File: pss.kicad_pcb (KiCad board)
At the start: 2 copper layers, 352 x 220 mm, 665 parts, among them J101 Conn_01x06_Socket, J102 Conn_01x02_Socket, J103 Conn_01x02_Socket, J104 Conn_01x02_Socket, J2001 Conn_01x06_Socket, J2002 Conn_01x06_Socket, J2101 Conn_01x06_Socket, J2801 Conn_01x06_Socket, K3501 ALFG2PF12, M2101 Fan, M2801 Fan, Q1401 DNLS350E, Q1901 DPLS350E, Q1902 DNLS350E, Q1903 DPLS350E, Q1904 DPLS350E, Q1905 DNLS350E, Q1906 DNLS350E, Q1907 TIP41C, Q1908 TIP42C, Q2201 DNLS350E, Q2202 DPLS350E, Q2203 TIP41C, Q2204 TIP42C, Q2301 DNLS350E, Q2302 DPLS350E, Q2303 TIP41C, Q2304 TIP42C, Q2401 DNLS350E, Q2402 DPLS350E, Q2403 TIP41C, Q2404 TIP42C, Q2501 DNLS350E, Q2502 DPLS350E, Q2503 TIP41C, Q2504 TIP42C, Q2601 DNLS350E, Q2602 DPLS350E, Q2603 TIP41C, Q2604 TIP42C, Q2701 DNLS350E, Q2702 DPLS350E, Q2703 TIP41C, Q2704 TIP42C, Q2901 DNLS350E, Q2902 DPLS350E, Q2903 TIP41C, Q2904 TIP42C, Q3001 DNLS350E, Q3002 DPLS350E, Q3003 TIP41C, Q3004 TIP42C, Q3101 DNLS350E, Q3102 DPLS350E, Q3103 TIP41C, Q3104 TIP42C, Q3201 DNLS350E, Q3202 DPLS350E, Q3203 TIP41C, Q3204 TIP42C, Q3301 DNLS350E, Q3302 DPLS350E, Q3303 TIP41C, Q3304 TIP42C, Q3401 DNLS350E, Q3402 DPLS350E, Q3403 TIP41C, Q3404 TIP42C, Q3501 DPLS350E, Q401 DNLS350E, Q402 DNLS350E, Q403 DPLS350E, Q404 DPLS350E, U1001 TLV9352, U1101 TLV9352, U1201 TLV9352, U1301 TLV9352, U1401 4081, U1402 4073, U1403 4073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

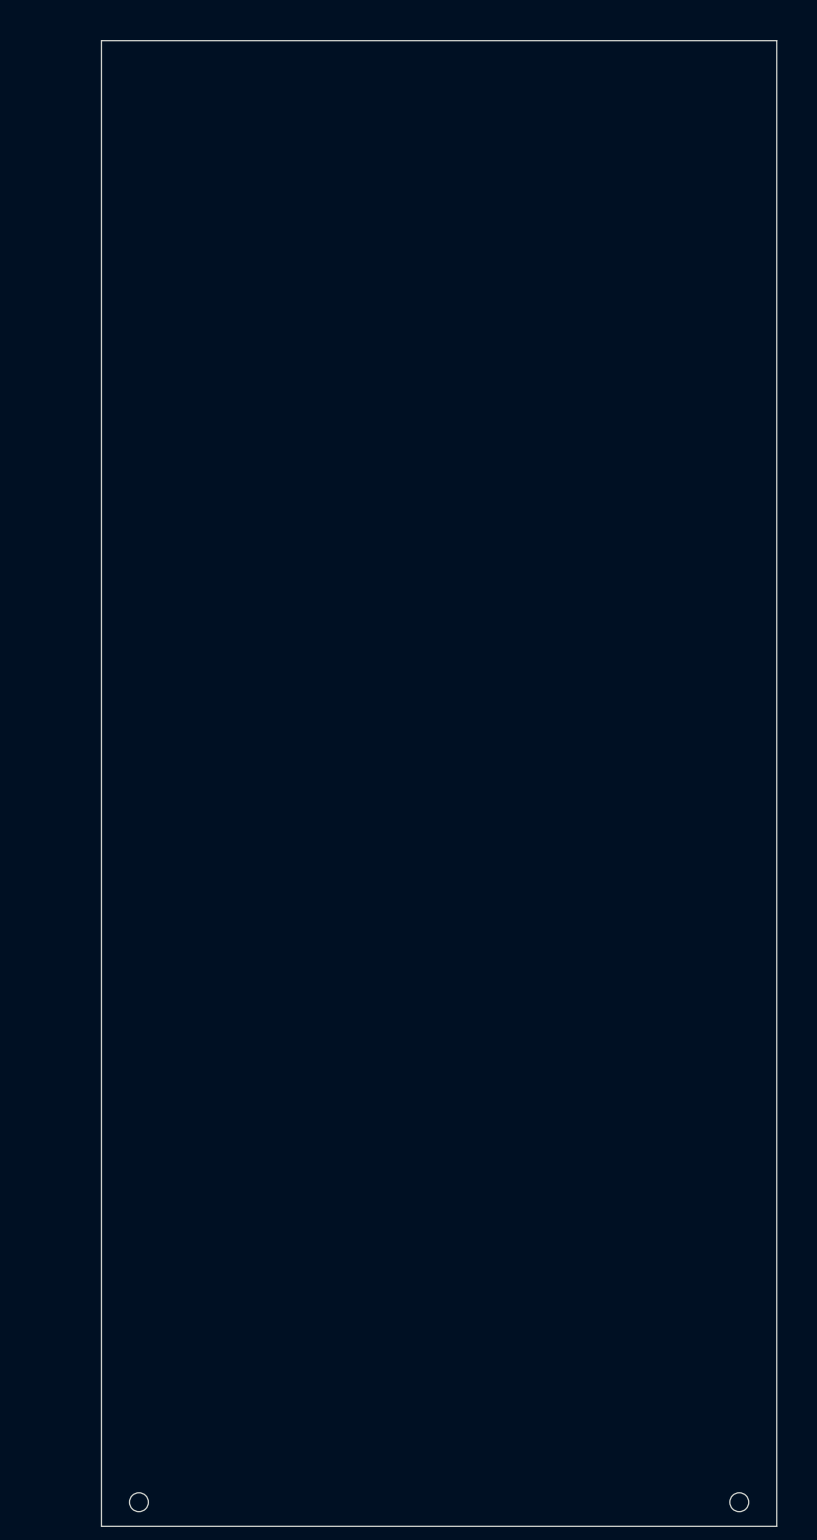
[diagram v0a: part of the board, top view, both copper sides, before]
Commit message: add pcb edge clearance keepout area
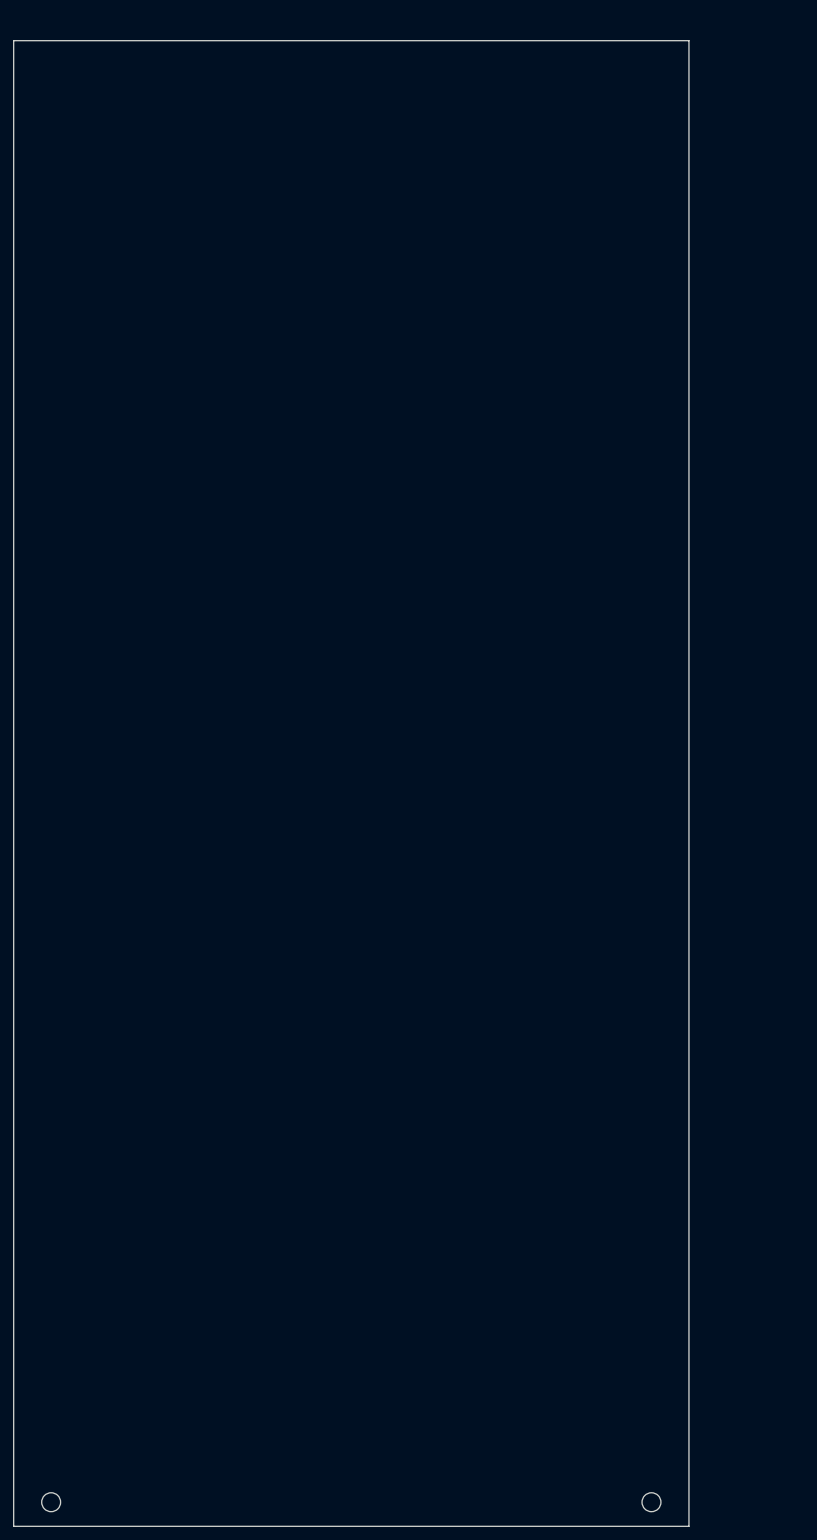
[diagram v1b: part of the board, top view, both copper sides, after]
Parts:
- moved REF** 13.0 mm to (129.4, 236.4)
- moved REF** 13.0 mm to (40.5, 236.4)
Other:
- board size 352 x 220 mm -> 365 x 220 mm

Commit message: add pcb mounting holes for stacking via M3x60 hexnuts
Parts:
- added REF**: MountingHole_3.2mm_M3, pss:MountingHole_3.2mm_M3, F.Cu at (320.0, 90.0)
- added REF**: MountingHole_3.2mm_M3, pss:MountingHole_3.2mm_M3, F.Cu at (380.0, 220.0)
- added REF**: MountingHole_3.2mm_M3, pss:MountingHole_3.2mm_M3, F.Cu at (380.0, 90.0)
- added REF**: MountingHole_3.2mm_M3, pss:MountingHole_3.2mm_M3, F.Cu at (205.0, 90.0)
- added REF**: MountingHole_3.2mm_M3, pss:MountingHole_3.2mm_M3, F.Cu at (205.0, 220.0)
- added REF**: MountingHole_3.2mm_M3, pss:MountingHole_3.2mm_M3, F.Cu at (320.0, 220.0)
- added REF**: MountingHole_3.2mm_M3, pss:MountingHole_3.2mm_M3, F.Cu at (115.0, 220.0)
- added REF**: MountingHole_3.2mm_M3, pss:MountingHole_3.2mm_M3, F.Cu at (55.0, 220.0)
- added REF**: MountingHole_3.2mm_M3, pss:MountingHole_3.2mm_M3, F.Cu at (55.0, 90.0)
- added REF**: MountingHole_3.2mm_M3, pss:MountingHole_3.2mm_M3, F.Cu at (265.0, 90.0)
- added REF**: MountingHole_3.2mm_M3, pss:MountingHole_3.2mm_M3, F.Cu at (115.0, 90.0)
- added REF**: MountingHole_3.2mm_M3, pss:MountingHole_3.2mm_M3, F.Cu at (265.0, 220.0)
- moved M2801 189.0 mm to (-3.88, -30.5), turned to 180 degrees
- moved JP2801 125.5 mm to (31.1, -73.8)
- moved TP2801 125.5 mm to (27.0, -74.0)
- moved TP2802 125.5 mm to (27.0, -71.0)
- moved TP2803 125.5 mm to (27.0, -67.9)
- moved TP2804 125.5 mm to (27.0, -64.8)
- moved TP2805 125.5 mm to (27.0, -61.8)
- moved TP2806 125.5 mm to (27.0, -58.8)
- moved HS2801 72.6 mm to (-3.88, -170.5)
- moved J2801 66.5 mm to (40.5, -111.7), turned to -90 degrees

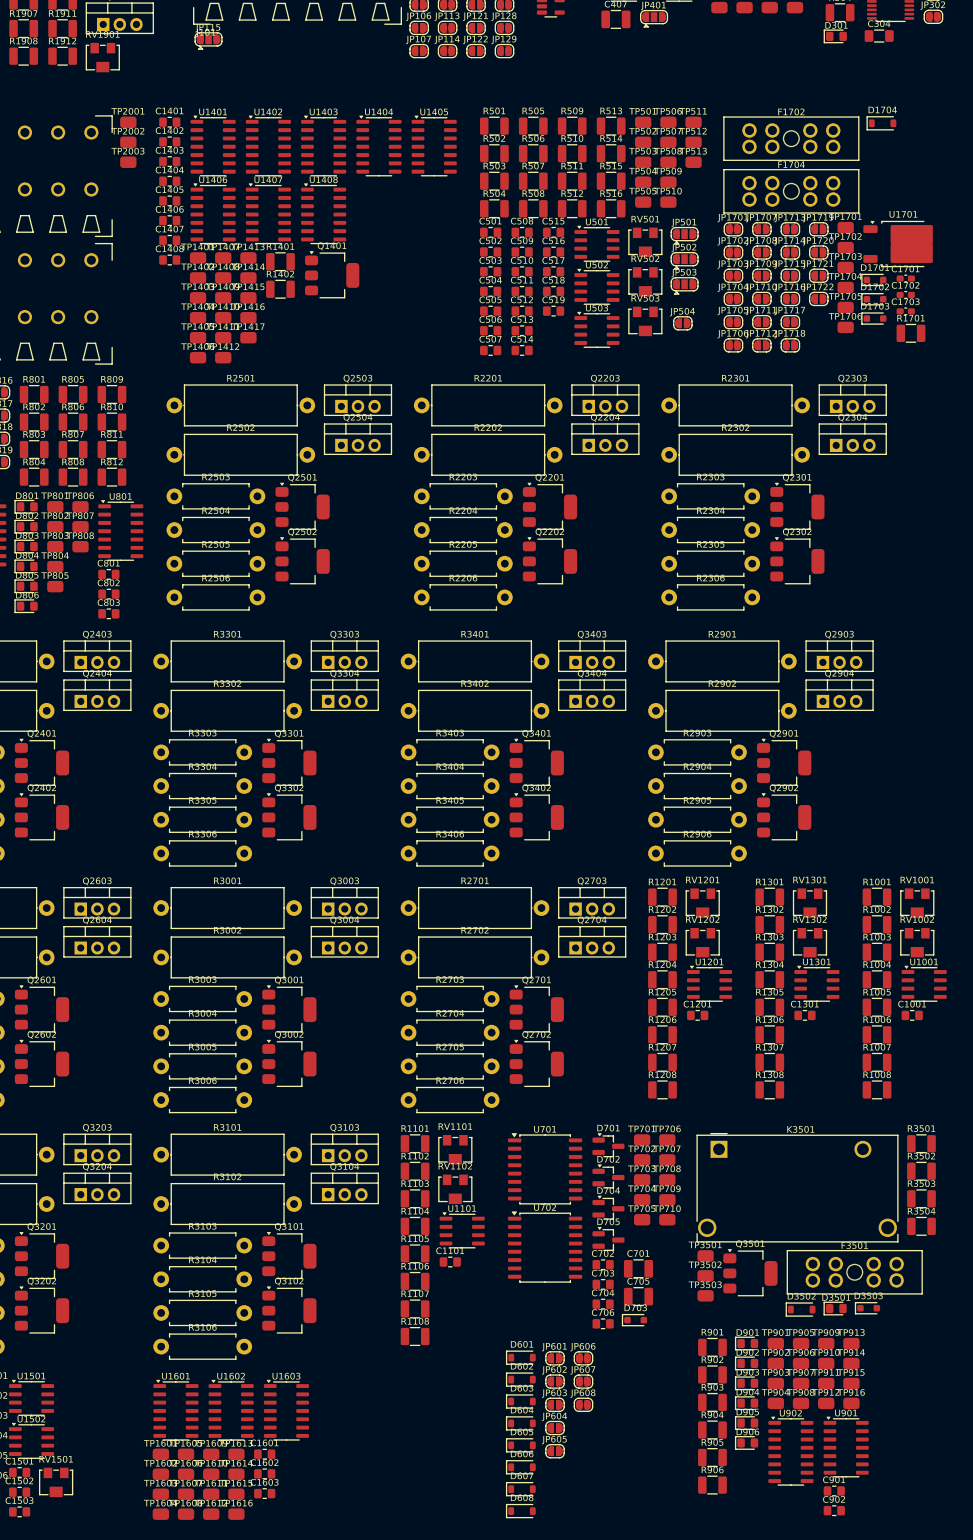
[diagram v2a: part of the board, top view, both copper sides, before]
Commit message: edit trimmer adjustment style to sideways
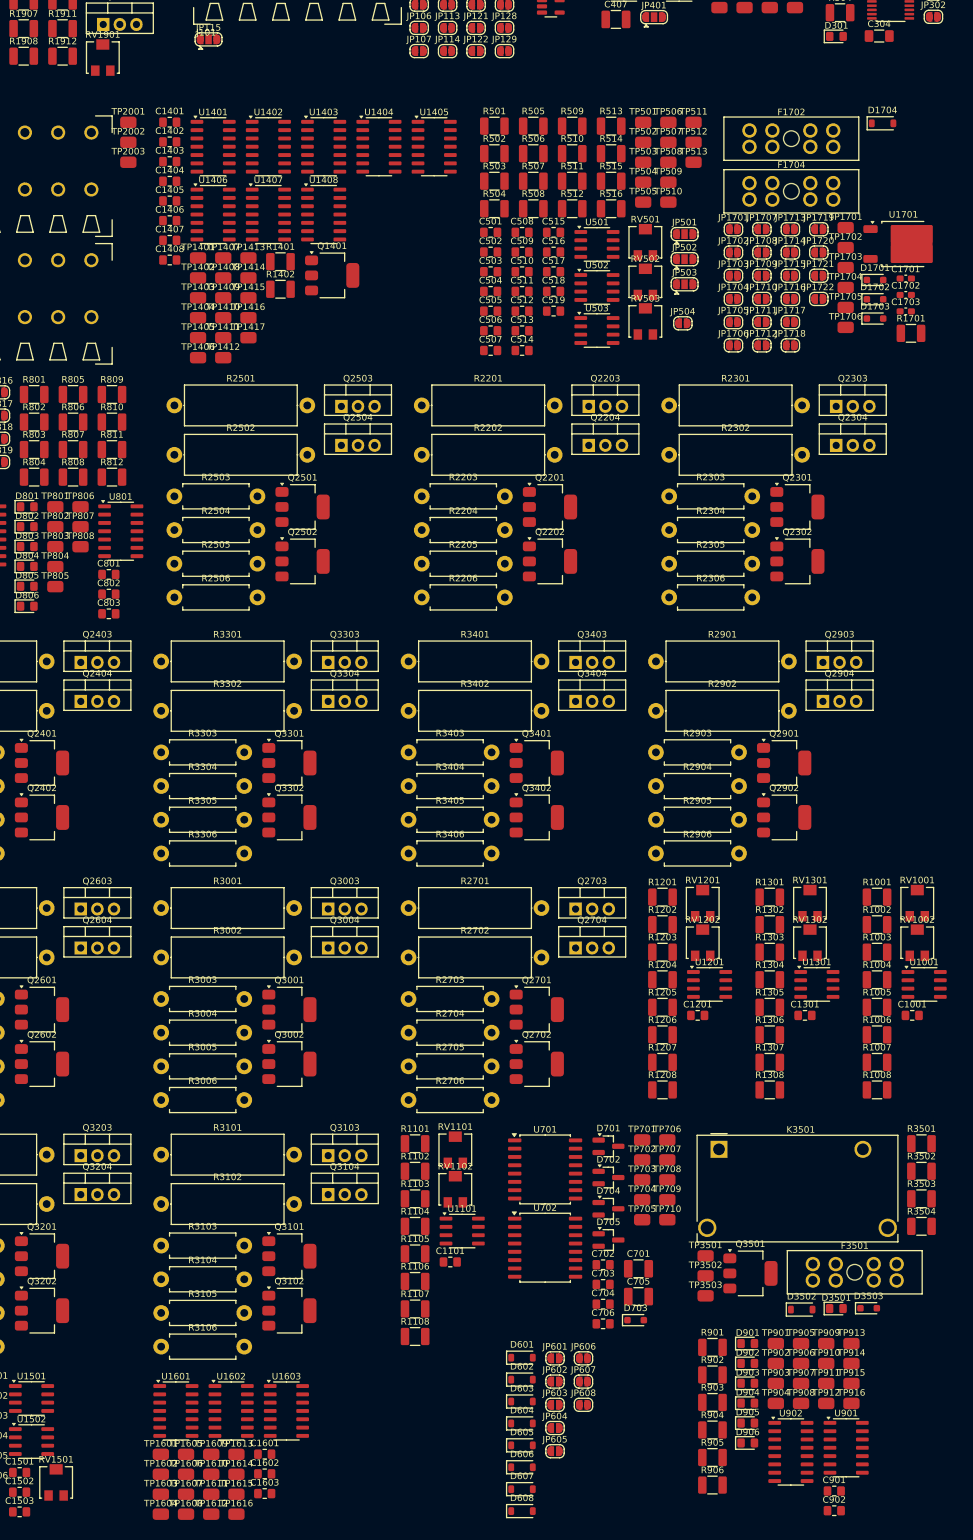
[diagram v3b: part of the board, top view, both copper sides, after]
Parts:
- RV1001, RV1002, RV1101, RV1102, RV1201, RV1202, RV1301, RV1302, RV1501, RV1901, RV501, RV502, RV503: footprint pss:Potentiometer_Bourns_PVG5A -> pss:Potentiometer_Bourns_PVG5H
